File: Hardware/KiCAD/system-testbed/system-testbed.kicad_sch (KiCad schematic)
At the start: 1 part, among them IC2 PCF8575PWR

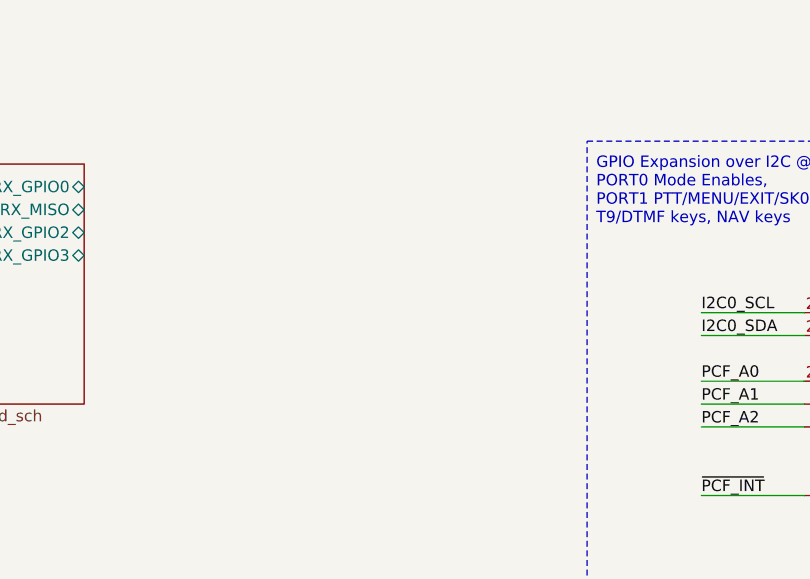
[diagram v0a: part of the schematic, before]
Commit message: feat: begin importing Battery Management System capture in new power subsystem sheet #3 #21
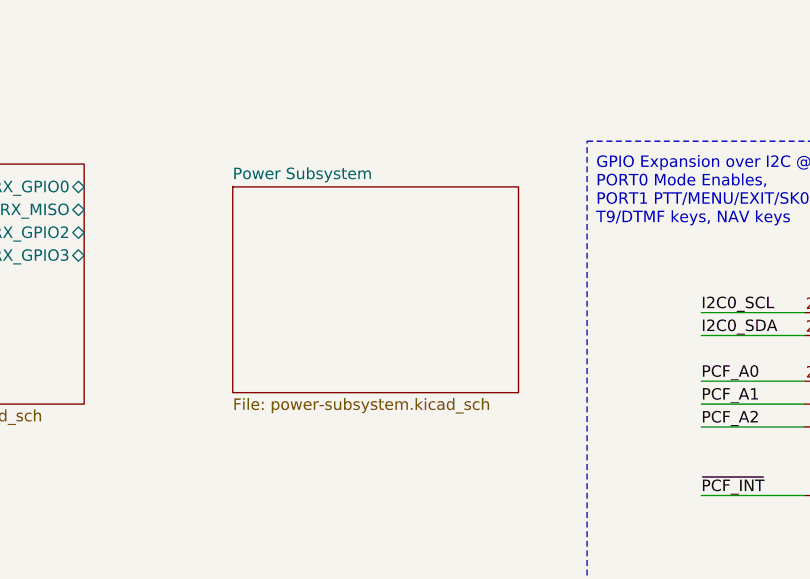
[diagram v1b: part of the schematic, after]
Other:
- added sheet Power Subsystem (power-subsystem.kicad_sch)
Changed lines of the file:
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@@
+	)
+	(sheet
+		(at 171.45 93.98)
+		(size 31.75 22.86)
+		(exclude_from_sim no)
+		(in_bom yes)
+		(on_board yes)
+		(dnp no)
+		(fields_autoplaced yes)
+		(stroke
+			(width 0.1524)
+			(type solid)
+		)
+		(fill
+			(color 255 229 191 1.0000)
+		)
+		(property "Sheetname" "Power Subsystem"
+			(at 171.45 93.2684 0)
+			(effects
+				(font
+					(size 1.27 1.27)
+				)
+				(justify left bottom)
+			)
+		)
+		(property "Sheetfile" "power-subsystem.kicad_sch"
+			(at 171.45 117.4246 0)
+			(effects
+				(font
+					(size 1.27 1.27)
+				)
+				(justify left top)
+			)
+		)
+		(instances
+			(project "system-testbed"
+				(path "/72756aea-0ff9-4757-9699-8d0f18588f6f"
+					(page "7")
+				)
+			)
+		)
 	)
 	(sheet

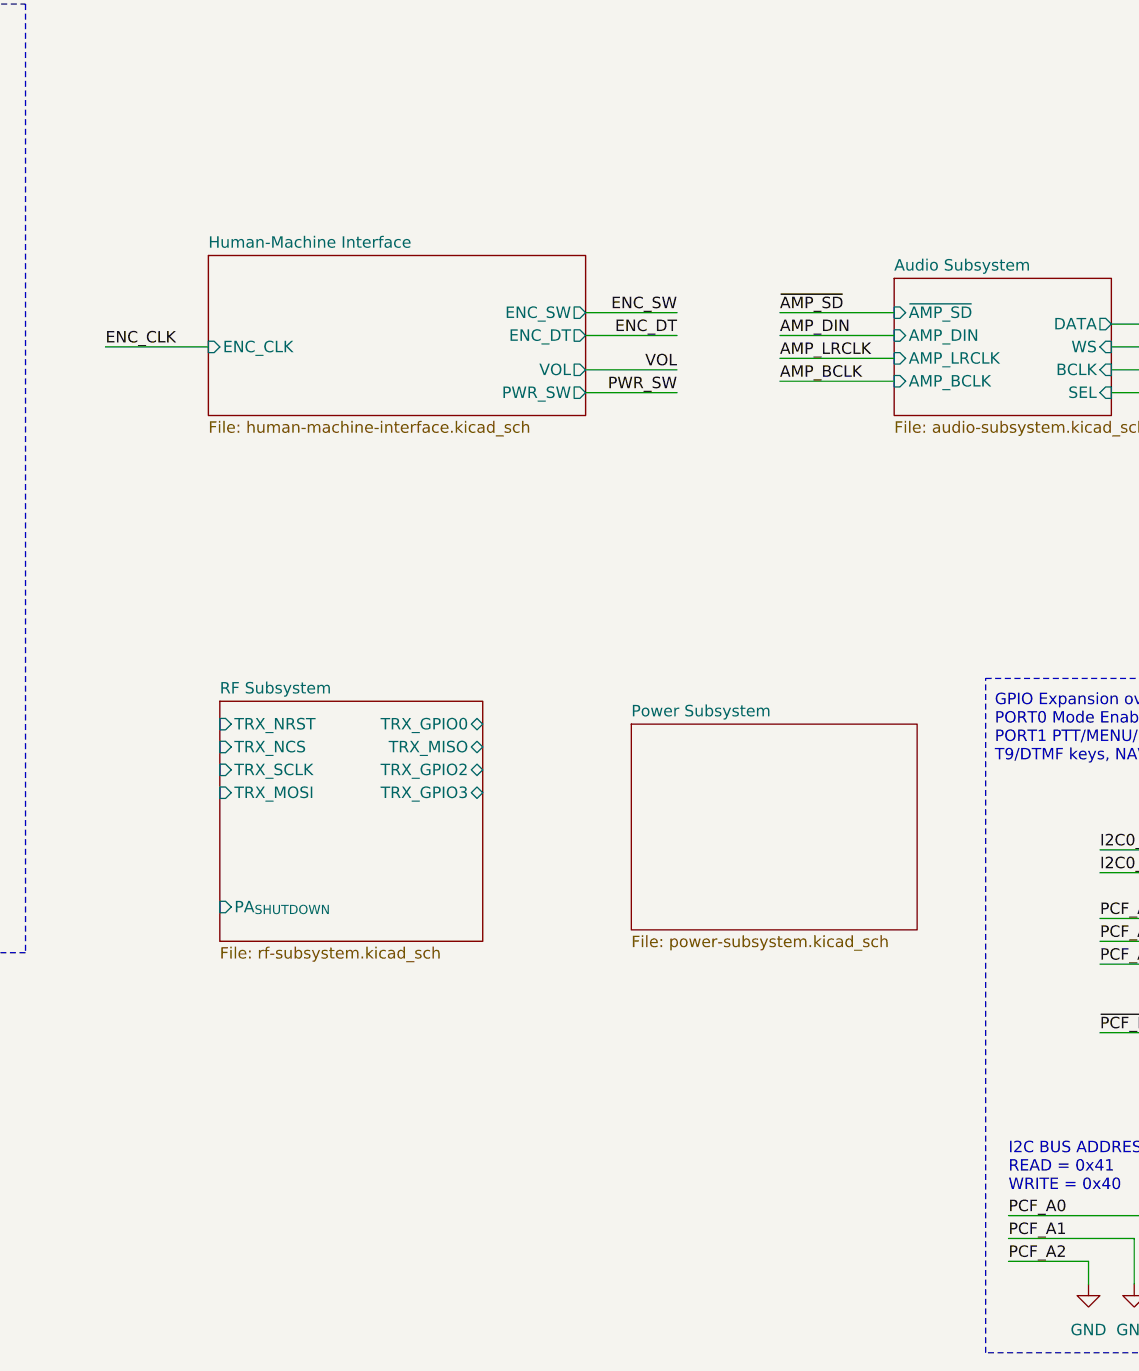
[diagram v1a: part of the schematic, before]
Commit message: chore: clear power subsystem schematic, restructure subsheets
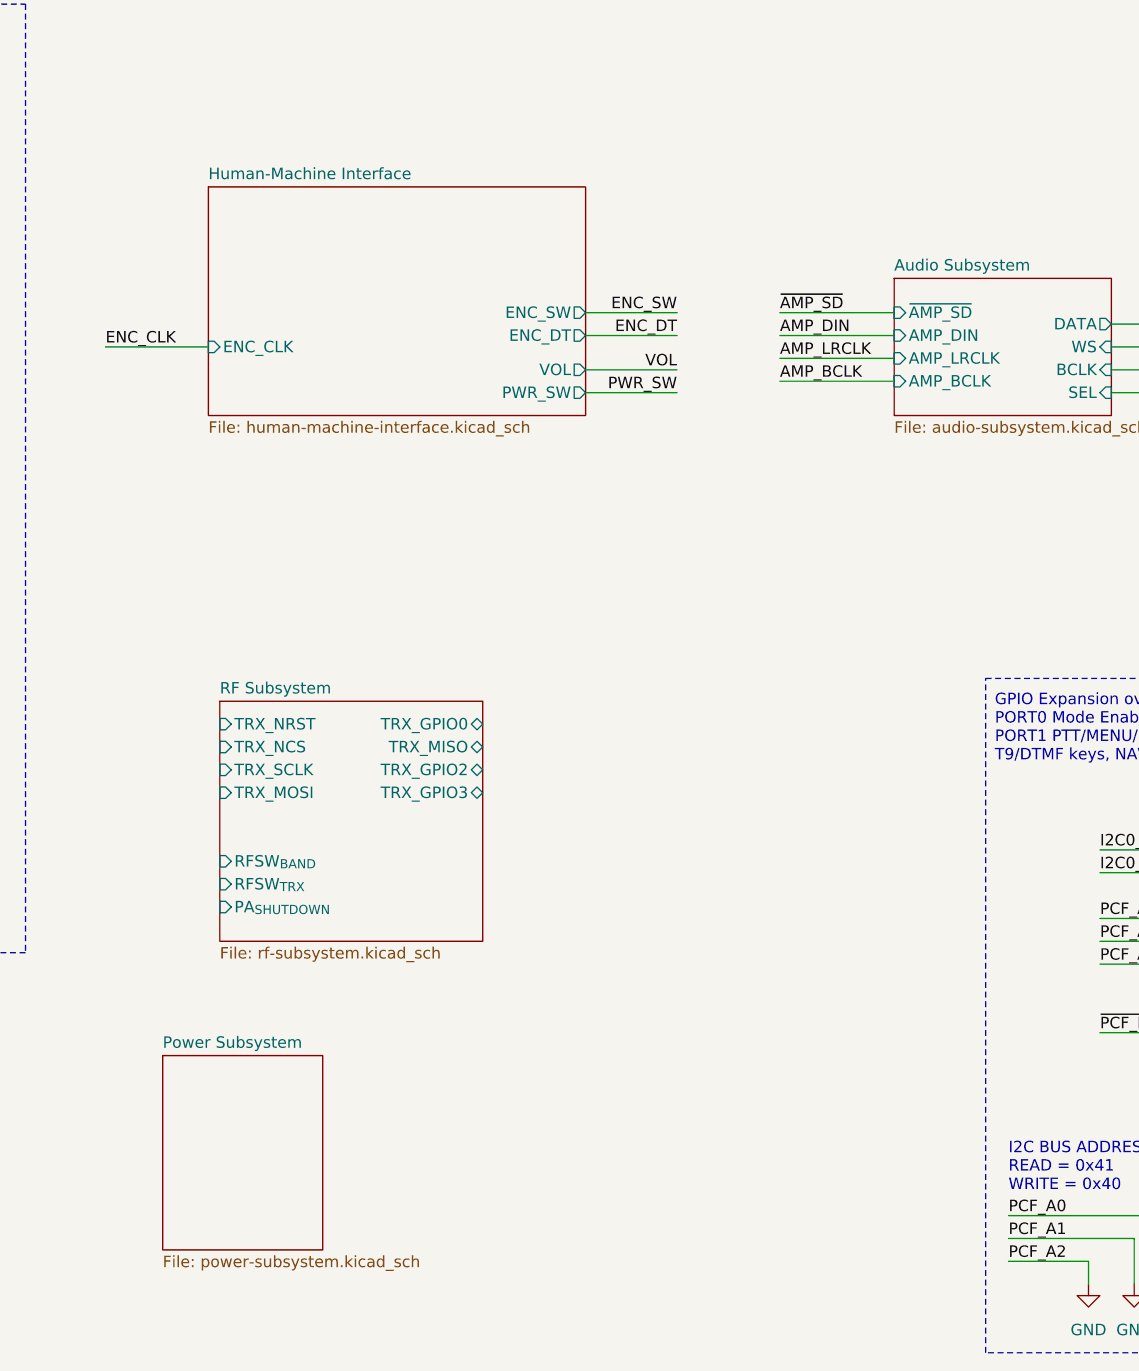
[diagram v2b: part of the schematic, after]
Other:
- sheet RF Subsystem ports: added RFSW_{BAND}, RFSW_{TRX}; removed none
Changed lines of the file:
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@@
+			)
+		)
+		(pin "RFSW_{TRX}" input
+			(at 125.73 111.76 180)
+			(effects
+				(font
+					(size 1.27 1.27)
+				)
+				(justify left)
+			)
+		)
+		(pin "RFSW_{BAND}" input
+			(at 125.73 109.22 180)
+			(effects
+				(font
+					(size 1.27 1.27)
+				)
+				(justify left)
 			)
 		)
@@
 	)
 	(sheet
-		(at 124.46 41.91)
-		(size 41.91 17.78)
+		(at 124.46 34.29)
+		(size 41.91 25.4)
 		(exclude_from_sim no)
 		(in_bom yes)
@@
 		)
 		(property "Sheetname" "Human-Machine Interface"
-			(at 124.46 41.1984 0)
+			(at 124.46 33.5784 0)
 			(effects
 				(font
@@
 			(project "system-testbed"
 				(path "/72756aea-0ff9-4757-9699-8d0f18588f6f"
-					(page "3")
+					(page "2")
 				)
 			)
@@
 	)
 	(sheet
-		(at 171.45 93.98)
-		(size 31.75 22.86)
+		(at 119.38 130.81)
+		(size 17.78 21.59)
 		(exclude_from_sim no)
 		(in_bom yes)
@@
 		)
 		(property "Sheetname" "Power Subsystem"
-			(at 171.45 93.2684 0)
+			(at 119.38 130.0984 0)
 			(effects
 				(font
@@
 		)
 		(property "Sheetfile" "power-subsystem.kicad_sch"
-			(at 171.45 117.4246 0)
+			(at 119.38 152.9846 0)
 			(effects
 				(font
@@
 			(project "system-testbed"
 				(path "/72756aea-0ff9-4757-9699-8d0f18588f6f"
-					(page "7")
+					(page "9")
 				)
 			)
@@
 			(project "system-testbed"
 				(path "/72756aea-0ff9-4757-9699-8d0f18588f6f"
-					(page "4")
+					(page "3")
 				)
 			)
@@
 			(project "system-testbed"
 				(path "/72756aea-0ff9-4757-9699-8d0f18588f6f"
-					(page "2")
-				)
-			)
+					(page "4")
+				)
+			)

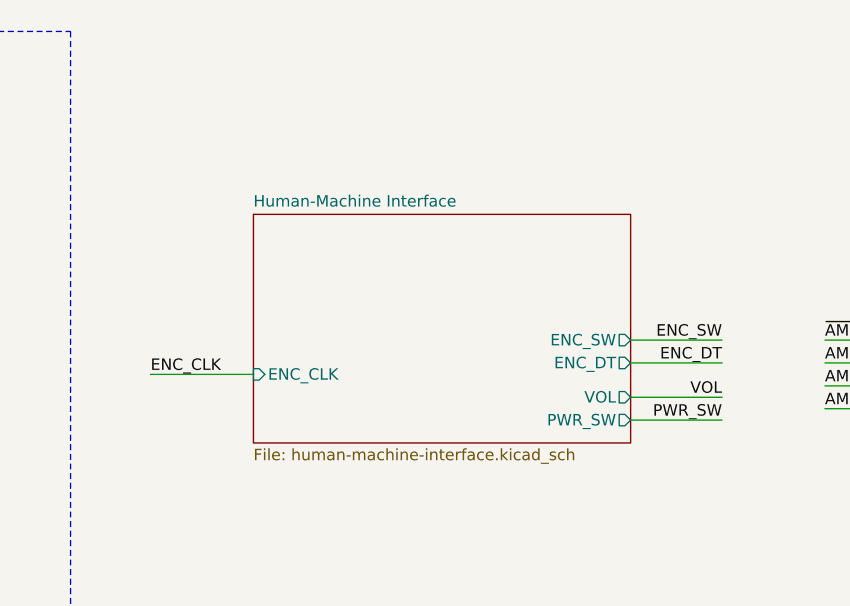
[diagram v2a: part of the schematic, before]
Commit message: feat: capture EYESPI display connectors #15
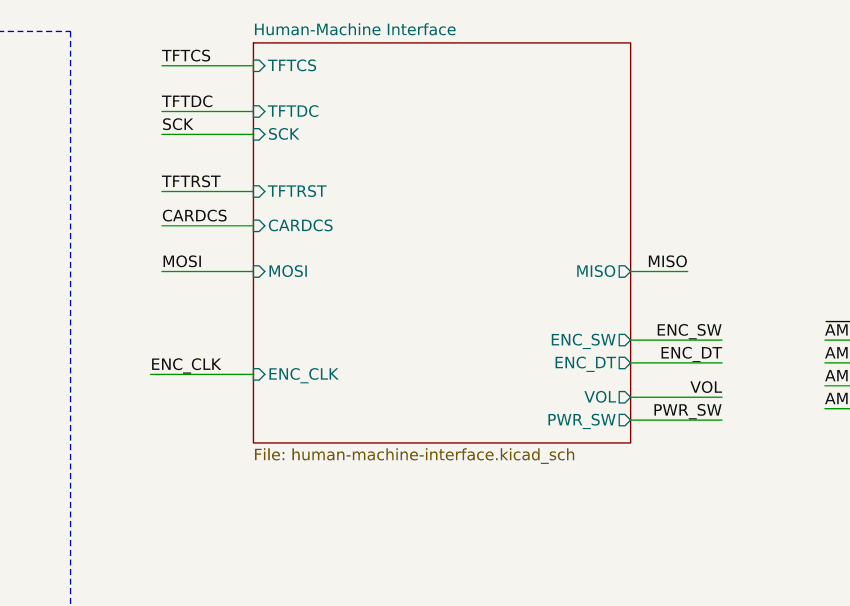
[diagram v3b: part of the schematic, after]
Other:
- sheet Human-Machine Interface ports: added CARDCS, MISO, MOSI, SCK, TFTCS, TFTDC, TFTRST; removed none
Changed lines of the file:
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@@
+	(wire
+		(pts
+			(xy 114.3 25.4) (xy 124.46 25.4)
+		)
+		(stroke
+			(width 0)
+			(type default)
+		)
+	)
 	(wire
 		(pts
@@
 	(wire
 		(pts
+			(xy 172.72 40.64) (xy 166.37 40.64)
+		)
+		(stroke
+			(width 0)
+			(type default)
+		)
+	)
+	(wire
+		(pts
 			(xy 187.96 48.26) (xy 200.66 48.26)
 		)
@@
 	(wire
 		(pts
+			(xy 114.3 35.56) (xy 124.46 35.56)
+		)
+		(stroke
+			(width 0)
+			(type default)
+		)
+	)
+	(wire
+		(pts
 			(xy 245.11 153.67) (xy 245.11 156.21)
 		)
@@
 	(wire
 		(pts
+			(xy 114.3 40.64) (xy 124.46 40.64)
+		)
+		(stroke
+			(width 0)
+			(type default)
+		)
+	)
+	(wire
+		(pts
 			(xy 266.7 115.57) (xy 255.27 115.57)
 		)
@@
 	(wire
 		(pts
+			(xy 114.3 31.75) (xy 124.46 31.75)
+		)
+		(stroke
+			(width 0)
+			(type default)
+		)
+	)
+	(wire
+		(pts
 			(xy 266.7 113.03) (xy 255.27 113.03)
 		)
@@
 	(wire
 		(pts
+			(xy 114.3 22.86) (xy 124.46 22.86)
+		)
+		(stroke
+			(width 0)
+			(type default)
+		)
+	)
+	(wire
+		(pts
 			(xy 255.27 123.19) (xy 266.7 123.19)
 		)
@@
 		(pts
 			(xy 255.27 140.97) (xy 267.97 140.97)
+		)
+		(stroke
+			(width 0)
+			(type default)
+		)
+	)
+	(wire
+		(pts
+			(xy 114.3 17.78) (xy 124.46 17.78)
 		)
 		(stroke
@@
 		)
 	)
+	(label "TFTCS"
+		(at 114.3 17.78 0)
+		(effects
+			(font
+				(size 1.27 1.27)
+			)
+			(justify left bottom)
+		)
+	)
 	(label "VOL"
 		(at 176.53 54.61 180)
@@
 		)
 	)
+	(label "MOSI"
+		(at 114.3 40.64 0)
+		(effects
+			(font
+				(size 1.27 1.27)
+			)
+			(justify left bottom)
+		)
+	)
 	(label "AMP_BCLK"
 		(at 187.96 55.88 0)
@@
 		)
 	)
+	(label "TFTDC"
+		(at 114.3 22.86 0)
+		(effects
+			(font
+				(size 1.27 1.27)
+			)
+			(justify left bottom)
+		)
+	)
+	(label "MISO"
+		(at 172.72 40.64 180)
+		(effects
+			(font
+				(size 1.27 1.27)
+			)
+			(justify right bottom)
+		)
+	)
+	(label "CARDCS"
+		(at 114.3 35.56 0)
+		(effects
+			(font
+				(size 1.27 1.27)
+			)
+			(justify left bottom)
+		)
+	)
 	(label "~{AMP_SD}"
 		(at 266.7 118.11 180)
@@
 		)
 	)
+	(label "SCK"
+		(at 114.3 25.4 0)
+		(effects
+			(font
+				(size 1.27 1.27)
+			)
+			(justify left bottom)
+		)
+	)
 	(label "I2C0_SCL"
 		(at 223.52 107.95 0)
@@
 	(label "~{PCF_INT}"
 		(at 223.52 128.27 0)
+		(effects
+			(font
+				(size 1.27 1.27)
+			)
+			(justify left bottom)
+		)
+	)
+	(label "TFTRST"
+		(at 114.3 31.75 0)
 		(effects
 			(font
@@
 	)
 	(sheet
-		(at 124.46 34.29)
-		(size 41.91 25.4)
+		(at 124.46 15.24)
+		(size 41.91 44.45)
 		(exclude_from_sim no)
 		(in_bom yes)
@@
 		)
 		(property "Sheetname" "Human-Machine Interface"
-			(at 124.46 33.5784 0)
+			(at 124.46 14.5284 0)
 			(effects
 				(font
@@
 			)
 		)
+		(pin "MOSI" input
+			(at 124.46 40.64 180)
+			(effects
+				(font
+					(size 1.27 1.27)
+				)
+				(justify left)
+			)
+		)
+		(pin "SCK" input
+			(at 124.46 25.4 180)
+			(effects
+				(font
+					(size 1.27 1.27)
+				)
+				(justify left)
+			)
+		)
+		(pin "TFTDC" input
+			(at 124.46 22.86 180)
+			(effects
+				(font
+					(size 1.27 1.27)
+				)
+				(justify left)
+			)
+		)
+		(pin "MISO" output
+			(at 166.37 40.64 0)
+			(effects
+				(font
+					(size 1.27 1.27)
+				)
+				(justify right)
+			)
+		)
+		(pin "TFTCS" input
+			(at 124.46 17.78 180)
+			(effects
+				(font
+					(size 1.27 1.27)
+				)
+				(justify left)
+			)
+		)
+		(pin "TFTRST" input
+			(at 124.46 31.75 180)
+			(effects
+				(font
+					(size 1.27 1.27)
+				)
+				(justify left)
+			)
+		)
+		(pin "CARDCS" input
+			(at 124.46 35.56 180)
+			(effects
+				(font
+					(size 1.27 1.27)
+				)
+				(justify left)
+			)
+		)

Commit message: feat: Power Subsystem Power Supply PCB Fixes #31
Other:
- sheet Power Subsystem ports: added *INT, *PG, SCL, SDA, STAT; removed none
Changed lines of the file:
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@@
 	)
 	(sheet
-		(at 119.38 130.81)
-		(size 17.78 21.59)
+		(at 53.34 147.32)
+		(size 33.02 20.32)
 		(exclude_from_sim no)
 		(in_bom yes)
@@
 		)
 		(property "Sheetname" "Power Subsystem"
-			(at 119.38 130.0984 0)
+			(at 53.34 146.6084 0)
 			(effects
 				(font
@@
 		)
 		(property "Sheetfile" "power-subsystem.kicad_sch"
-			(at 119.38 152.9846 0)
+			(at 53.34 168.2246 0)
 			(effects
 				(font
@@
 			)
 		)
+		(pin "*INT" output
+			(at 86.36 152.4 0)
+			(effects
+				(font
+					(size 1.27 1.27)
+				)
+				(justify right)
+			)
+		)
+		(pin "SDA" input
+			(at 53.34 152.4 180)
+			(effects
+				(font
+					(size 1.27 1.27)
+				)
+				(justify left)
+			)
+		)
+		(pin "STAT" output
+			(at 86.36 156.21 0)
+			(effects
+				(font
+					(size 1.27 1.27)
+				)
+				(justify right)
+			)
+		)
+		(pin "SCL" bidirectional
+			(at 86.36 160.02 0)
+			(effects
+				(font
+					(size 1.27 1.27)
+				)
+				(justify right)
+			)
+		)
+		(pin "*PG" output
+			(at 86.36 163.83 0)
+			(effects
+				(font
+					(size 1.27 1.27)
+				)
+				(justify right)
+			)
+		)

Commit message: feat: testing commit
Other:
- note added: "THE CUBE"
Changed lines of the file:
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@@
+	)
+	(rectangle
+		(start 15.24 177.165)
+		(end 35.56 196.215)
+		(stroke
+			(width 0.254)
+			(type solid)
+		)
+		(fill
+			(type none)
+		)
 	)
 	(rectangle
@@
 			)
 			(justify left top)
+		)
+	)
+	(text "THE CUBE"
+		(exclude_from_sim no)
+		(at 25.654 187.706 0)
+		(effects
+			(font
+				(size 2.54 2.54)
+				(thickness 0.508)
+				(bold yes)
+			)
 		)
 	)
@@
 	)
 	(sheet
-		(at 53.34 147.32)
+		(at 125.73 139.7)
 		(size 33.02 20.32)
 		(exclude_from_sim no)
@@
 		)
 		(property "Sheetname" "Power Subsystem"
-			(at 53.34 146.6084 0)
+			(at 125.73 138.9884 0)
 			(effects
 				(font
@@
 		)
 		(property "Sheetfile" "power-subsystem.kicad_sch"
-			(at 53.34 168.2246 0)
+			(at 125.73 160.6046 0)
 			(effects
 				(font
@@
 		)
 		(pin "*INT" output
-			(at 86.36 152.4 0)
+			(at 158.75 144.78 0)
 			(effects
 				(font
@@
 		)
 		(pin "SDA" input
-			(at 53.34 152.4 180)
+			(at 125.73 144.78 180)
 			(effects
 				(font
@@
 		)
 		(pin "STAT" output
-			(at 86.36 156.21 0)
+			(at 158.75 148.59 0)
 			(effects
 				(font
@@
 		)
 		(pin "SCL" bidirectional
-			(at 86.36 160.02 0)
+			(at 158.75 152.4 0)
 			(effects
 				(font
@@
 		)
 		(pin "*PG" output
-			(at 86.36 163.83 0)
-			(effects
-				(font
+			(at 158.75 156.21 0)
+			(effects
+				(font
